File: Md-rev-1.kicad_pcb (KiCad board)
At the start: 2 copper layers, 50 x 21.5 mm, 29 parts, among them J1 USB_C_Receptacle_USB2.0, J2 54-00177, U1 MCP73831-2-OT, U2 MAX9814

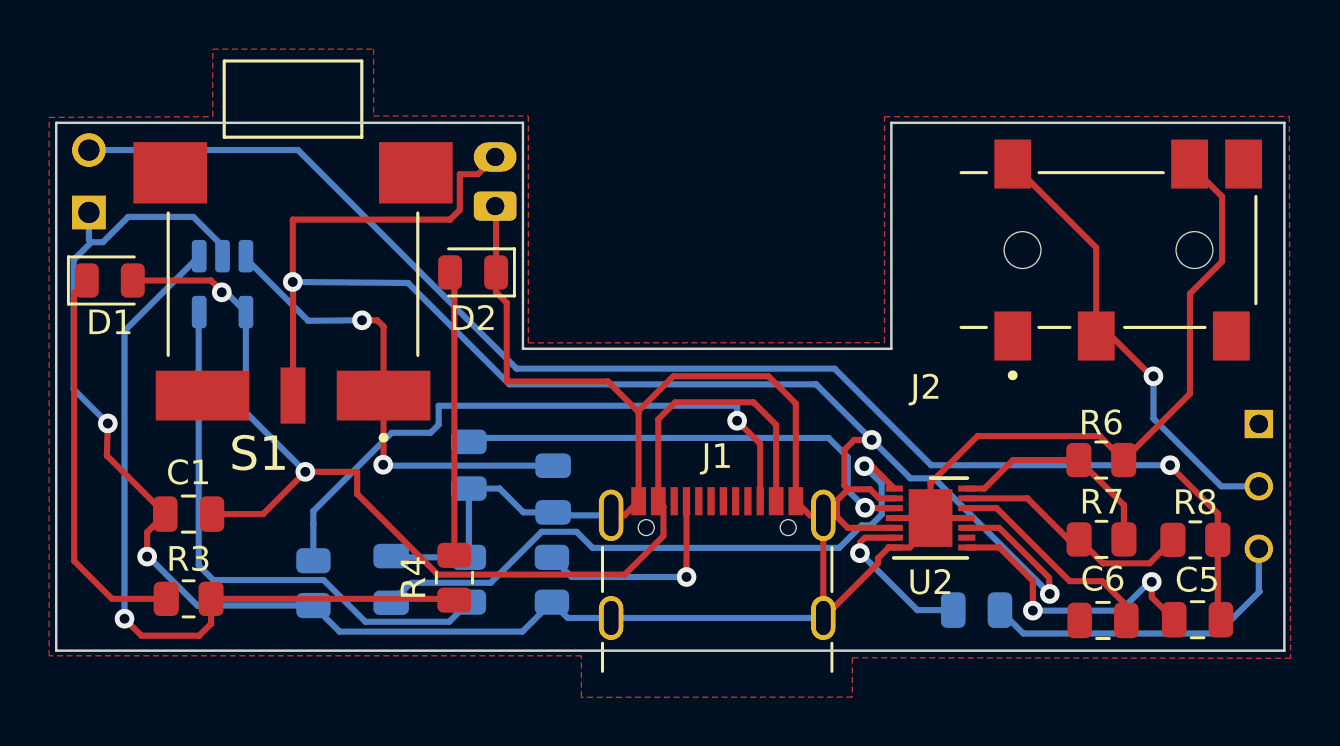
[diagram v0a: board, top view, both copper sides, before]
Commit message: Reorganized the board to meet some of the design rules listed from similar pcb's
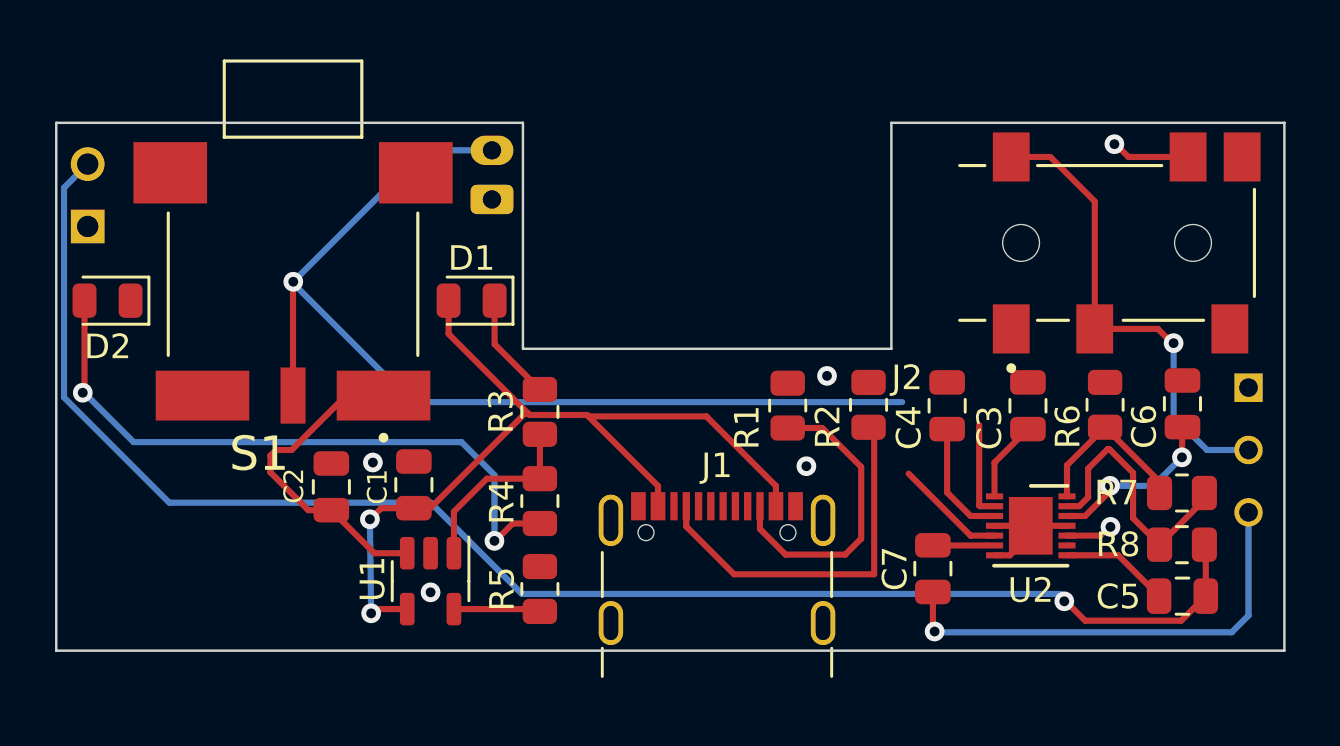
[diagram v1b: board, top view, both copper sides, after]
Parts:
- removed the ? at (179.0, 118.9)
- removed the ? at (147.9, 107.5)
- removed the ? at (179.0, 116.4)
- removed the ? at (131.3, 105.2)
- removed the ? at (179.0, 121.5)
- removed the ? at (147.9, 105.5)
- removed the ? at (131.3, 107.8)
- added ?: , , F.Cu at (178.5, 117.5)
- added ?: , , F.Cu at (178.5, 114.9)
- added ?: , , F.Cu at (147.7, 105.3)
- added ?: , , F.Cu at (147.7, 107.3)
- added ?: , , F.Cu at (178.5, 120.0)
- added ?: , , F.Cu at (131.3, 105.8)
- added ?: , , F.Cu at (131.3, 108.4)
- C2, C3, C4, C7, R1, R2, R5, U1: moved to F.Cu
- moved C3 26.9 mm to (169.6, 115.7)
- moved R1 20.6 mm to (159.8, 115.7), turned to 90 degrees
- moved C4 19.6 mm to (166.3, 115.7), turned to -90 degrees
- moved R3 16.2 mm to (149.7, 115.9), turned to 90 degrees
- moved D2 14.9 mm to (132.1, 111.4)
- moved U1 14.8 mm to (145.2, 122.8)
- moved D1 14.8 mm to (146.9, 111.4), turned to 180 degrees
- moved R2 14.7 mm to (163.1, 115.6), turned to 90 degrees
- moved C6 9.39 mm to (175.8, 115.6), turned to -90 degrees
- moved C1 9.25 mm to (144.6, 118.9), turned to -90 degrees
- moved C2 9.03 mm to (141.2, 119.0), turned to 90 degrees
- moved R4 4.67 mm to (149.7, 119.5), turned to -90 degrees
- moved U2 4.09 mm to (169.7, 120.5)
- moved R7 3.78 mm to (175.8, 119.2), turned to 0 degrees
- moved R5 2.91 mm to (149.7, 123.1)
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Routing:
- net GND: track 134.2 -> 9.59 mm, vias 2 -> 5
- net Net-(U1-STAT): track 31.0 -> 7.55 mm, vias 1 -> 0
- net Net-(U2-CT): track 25.9 -> 3.30 mm, vias 1 -> 0
- net Net-(U1-PROG): track 22.6 -> 3.54 mm
- net Net-(D2-A): track 11.6 -> 27.0 mm, vias 0 -> 2
- net /GAIN: track 67.5 -> 52.5 mm, vias 3 -> 2
- net Net-(U2-CG): track 19.4 -> 4.91 mm, vias 1 -> 0
- net Net-(J1-CC2): track 25.8 -> 12.3 mm, vias 1 -> 0
- net /5V: track 48.6 -> 36.7 mm
- net Net-(D1-K): track 16.0 -> 4.38 mm
- net Net-(U2-MICIN): track 11.9 -> 4.44 mm, vias 2 -> 0
- net Net-(J1-CC1): track 8.90 -> 15.4 mm, vias 1 -> 0
- net Net-(U1-V_{BAT}): track 19.5 -> 13.2 mm, vias 2 -> 0
- net Net-(C5-Pad1): track 57.0 -> 63.1 mm
- net /OUTPUT: track 13.4 -> 19.3 mm, vias 0 -> 1
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- removed copper zone on F.Cu, net GND

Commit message: updated the final PCB
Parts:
- removed the ? at (178.5, 117.5)
- removed the ? at (178.5, 114.9)
- removed the ? at (147.7, 105.3)
- removed the ? at (147.7, 107.3)
- removed the ? at (178.5, 120.0)
- removed the ? at (131.3, 105.8)
- removed the ? at (131.3, 108.4)
- added ?: , , F.Cu at (131.3, 108.0)
- added ?: , , F.Cu at (147.8, 106.0)
- added ?: , , F.Cu at (179.0, 114.7)
- added ?: , , F.Cu at (147.8, 108.0)
- added ?: , , F.Cu at (179.0, 119.8)
- added ?: , , F.Cu at (131.3, 105.5)
- added ?: , , F.Cu at (179.0, 117.3)
- added C8: 2.2uF, Capacitor_SMD:C_0805_2012Metric, F.Cu at (176.1, 126.3)
- added CN1: JSTPH, Connector_JST:JST_PH_S2B-PH-K_1x02_P2.00mm_Horizontal, F.Cu at (161.1, 87.7)
- added MK1: CMA-4544PF-W, CMA-4544PF-W:MIC_CMA-4544PF-W, F.Cu at (116.9, 96.4)
- added R9: 3352T-1-201LF, 3352T_1_201LF (1):TRIM_3352T-1-201LF, F.Cu at (189.6, 106.0)
- C3: value 0.1uF -> 2.2uF
- C4: value 2.2uF -> 10uF
- C7: value 10uF -> 0.1uF
- R6: value 100k -> 2.2K
- R8: value 2.2K -> 100k
- U2: value MAX9814 -> max9814etd+t; footprint Package_DFN_QFN:DFN-14-1EP_3x3mm_P0.4mm_EP1.78x2.35mm -> MAX9814etd+T:21-0137I_T1433-2_MXM
- moved C4 11.3 mm to (169.6, 126.4)
- moved C7 1.34 mm to (165.5, 121.0), turned to 0 degrees
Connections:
- C3 pad 2: Net-(U2-CT) -> Net-(U2-CG)
- C4 pad 1: GND -> /OUTPUT
- C4 pad 2: Net-(U2-CG) -> Net-(U2-MICOUT)
- C5 pad 1: Net-(C5-Pad1) -> GND
- C5 pad 2: Net-(U2-MICIN) -> Net-(U2-CT)
- C7 pad 1: Net-(U2-MICOUT) -> Net-(U2-MICIN)
- C7 pad 2: /OUTPUT -> VDD
- R6 pad 1: GND -> VDD
- R6 pad 2: Net-(U2-TH) -> Net-(U2-MICBIAS)
- R7 pad 1: Net-(U2-TH) -> Net-(U2-MICBIAS)
- R7 pad 2: Net-(U2-MICBIAS) -> Net-(U2-TH)
- R8 pad 1: Net-(C5-Pad1) -> Net-(U2-TH)
- R8 pad 2: Net-(U2-MICBIAS) -> GND
- S1 pad 1: Net-(U1-V_{BAT}) -> unconnected-(S1-Pad1)
- S1 pad 2: /GAIN -> /VBAT
- S1 pad 3: unconnected-(S1-Pad3) -> Net-(U1-V_{BAT})
- U2 pad 10: /GAIN -> VDD
- U2 pad 11: GND -> unconnected-(U2-NC-Pad11)
- U2 pad 2: /GAIN -> VDD
- U2 pad 4: GND -> unconnected-(U2-NC-Pad4)
- U2 pad 5: /GAIN -> VDD
- U2 pad 9: /A/R -> unconnected-(U2-A/R-Pad9)
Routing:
- net Net-(C5-Pad1): track 63.1 -> 0.00 mm, vias 1 -> 0
- net /GAIN: track 52.5 -> 0.00 mm, vias 2 -> 0
- net GND: track 9.59 -> 32.5 mm, vias 5 -> 4
- net /OUTPUT: track 19.3 -> 0.00 mm, vias 1 -> 0
- net /VBAT: track 0.00 -> 11.2 mm
- net Net-(U2-MICBIAS): track 11.0 -> 0.00 mm
- net VDD: track 0.00 -> 10.3 mm, vias 0 -> 1
- net Net-(J2-Pad2): track 19.5 -> 9.34 mm, vias 1 -> 0
- net Net-(U2-BIAS): track 7.14 -> 0.00 mm, vias 2 -> 0
- net Net-(U2-TH): track 7.05 -> 0.00 mm
- net Net-(U2-CG): track 4.91 -> 0.00 mm
- net Net-(U2-MICIN): track 4.44 -> 0.00 mm
- net Net-(U1-V_{BAT}): track 13.2 -> 17.0 mm
- net Net-(U2-CT): track 3.30 -> 0.00 mm
- net Net-(U2-MICOUT): track 2.16 -> 0.00 mm

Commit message: final save
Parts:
- removed the ? at (131.3, 108.0)
- removed the ? at (147.8, 106.0)
- removed the ? at (179.0, 114.7)
- removed the ? at (147.8, 108.0)
- removed the ? at (179.0, 119.8)
- removed the ? at (131.3, 105.5)
- removed the ? at (179.0, 117.3)
- removed CN1: JSTPH, Connector_JST:JST_PH_S2B-PH-K_1x02_P2.00mm_Horizontal
- removed MK1: CMA-4544PF-W, CMA-4544PF-W:MIC_CMA-4544PF-W
- removed R9: 3352T-1-201LF, 3352T_1_201LF (1):TRIM_3352T-1-201LF
- added ?: , , F.Cu at (178.9, 119.3)
- added ?: , , F.Cu at (178.9, 124.3)
- added ?: , , F.Cu at (131.4, 107.7)
- added ?: , , F.Cu at (147.8, 105.0)
- added ?: , , F.Cu at (131.4, 105.1)
- added ?: , , F.Cu at (147.8, 107.0)
- added ?: , , F.Cu at (178.9, 121.8)
- added FB1: FERRITE, LI0805H151R_10:IND_LI0805H151R-10_LRD, F.Cu at (154.7, 114.7)
- added FB2: FERRITE, LI0805H151R_10:IND_LI0805H151R-10_LRD, F.Cu at (176.2, 121.9)
- moved C5 12.4 mm to (166.2, 115.7), turned to -90 degrees
- moved R8 8.61 mm to (169.4, 115.6), turned to 90 degrees
- moved C4 6.44 mm to (165.3, 121.7), turned to 0 degrees
- moved C7 6.36 mm to (171.0, 124.1)
- moved C3 5.84 mm to (165.3, 119.6), turned to 0 degrees
- moved R7 4.88 mm to (172.5, 115.7), turned to -90 degrees
- moved R6 2.90 mm to (175.6, 115.7), turned to 90 degrees
- moved C8 2.29 mm to (176.2, 124.1)
- moved C6 2.15 mm to (178.0, 115.7)
- moved U2 1.68 mm to (171.3, 120.0)
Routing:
- net VDD: track 10.3 -> 81.8 mm, vias 1 -> 4
- net GND: track 32.5 -> 60.7 mm, vias 4 -> 13
- net /OUTPUT: track 0.00 -> 16.5 mm
- net Net-(J2-Pad2): track 9.34 -> 22.5 mm, vias 0 -> 1
- net /VBAT: track 11.2 -> 24.1 mm, vias 0 -> 2
- net Net-(U2-MICBIAS): track 0.00 -> 8.45 mm
- net Net-(U2-BIAS): track 0.00 -> 6.47 mm
- net Net-(U2-TH): track 0.00 -> 6.31 mm
- net Net-(U1-V_{BAT}): track 17.0 -> 12.4 mm
- net Net-(U2-CT): track 0.00 -> 4.47 mm
- net Net-(U2-MICIN): track 0.00 -> 3.97 mm
- net Net-(U2-MICOUT): track 0.00 -> 3.92 mm
- net Net-(U2-CG): track 0.00 -> 3.56 mm
- added copper zone on B.Cu, net GND
- added copper zone on F.Cu, net GND

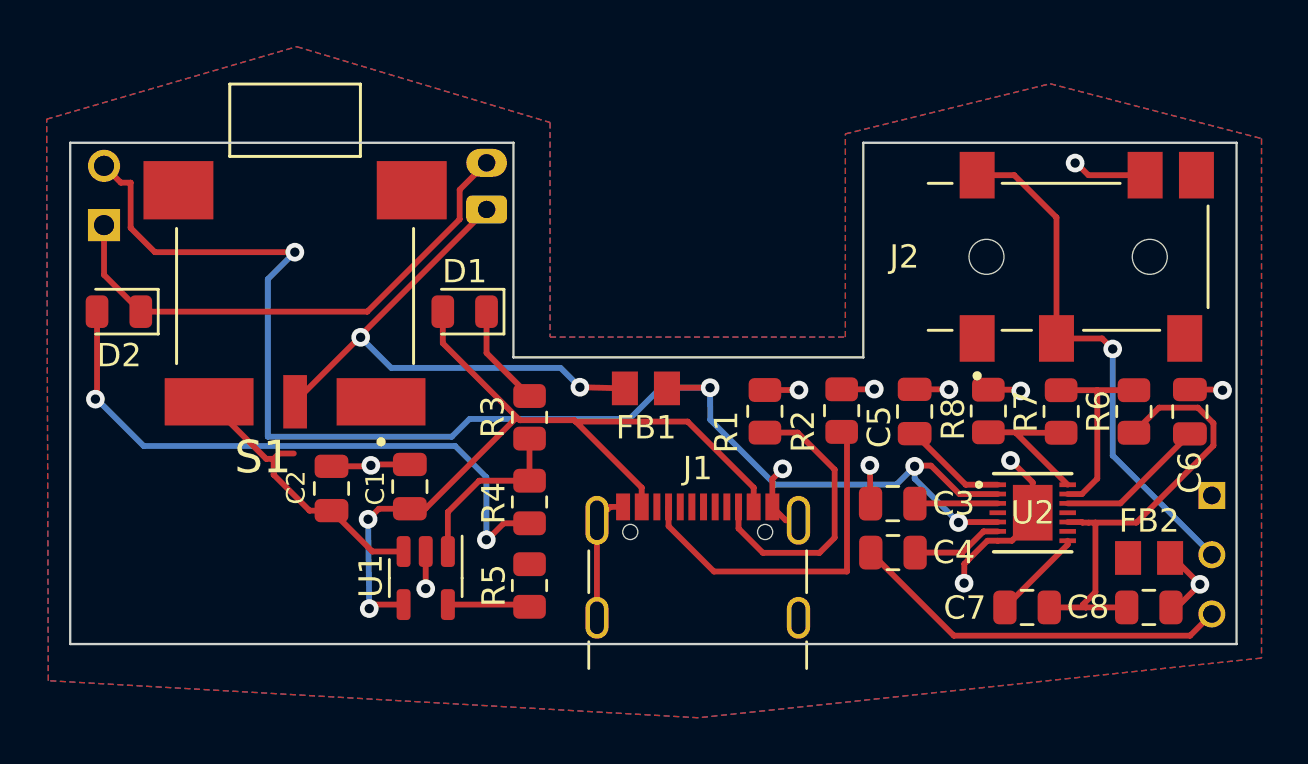
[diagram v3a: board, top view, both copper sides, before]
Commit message: added fabrication file for pick and place
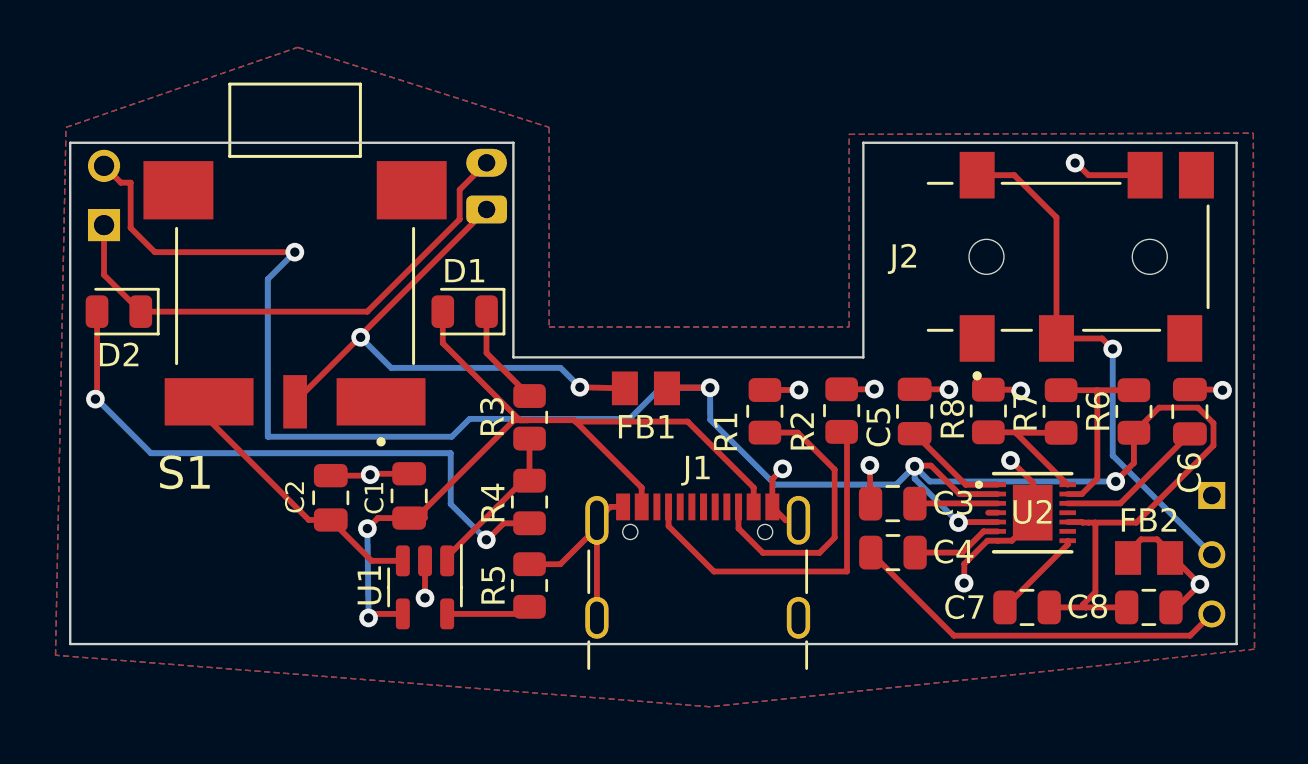
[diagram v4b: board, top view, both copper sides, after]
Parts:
- moved C1 0.40 mm to (144.5, 119.3)
- moved C2 0.40 mm to (141.2, 119.4)
- moved U1 0.40 mm to (145.2, 123.2)
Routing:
- net VDD: track 81.8 -> 93.1 mm, vias 4 -> 5
- net GND: track 60.7 -> 67.3 mm
- net /5V: track 36.7 -> 37.7 mm
- net Net-(U1-V_{BAT}): track 12.4 -> 11.6 mm
- net Net-(U1-STAT): track 7.55 -> 6.86 mm

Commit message: updated the schematic and the PCB
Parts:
- removed the ? at (178.9, 119.3)
- removed the ? at (178.9, 124.3)
- removed the ? at (131.4, 107.7)
- removed the ? at (147.8, 105.0)
- removed the ? at (131.4, 105.1)
- removed the ? at (147.8, 107.0)
- removed the ? at (178.9, 121.8)
- added ?: , , F.Cu at (179.0, 124.5)
- added ?: , , F.Cu at (147.9, 105.0)
- added ?: , , F.Cu at (131.4, 105.2)
- added ?: , , F.Cu at (131.4, 107.7)
- added ?: , , F.Cu at (147.9, 107.0)
- added ?: , , F.Cu at (179.0, 121.9)
- added ?: , , F.Cu at (179.0, 119.4)
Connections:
- C7 pad 2: VDD -> Net-(C7-Pad2)
- R6 pad 1: VDD -> Net-(C7-Pad2)
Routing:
- net Net-(C7-Pad2): track 0.00 -> 67.8 mm, vias 0 -> 2
- net Net-(J2-Pad2): track 22.5 -> 23.6 mm
- net GND: track 67.3 -> 67.9 mm
- net Net-(U2-BIAS): track 6.47 -> 7.01 mm
- removed copper zone on B.Cu, net GND
- removed copper zone on F.Cu, net GND
